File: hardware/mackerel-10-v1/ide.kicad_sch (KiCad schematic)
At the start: 12 parts, among them J14 Screw_Terminal_01x04, J3 Conn_02x20_Odd_Even, U12 74HC245, U13 74HC245

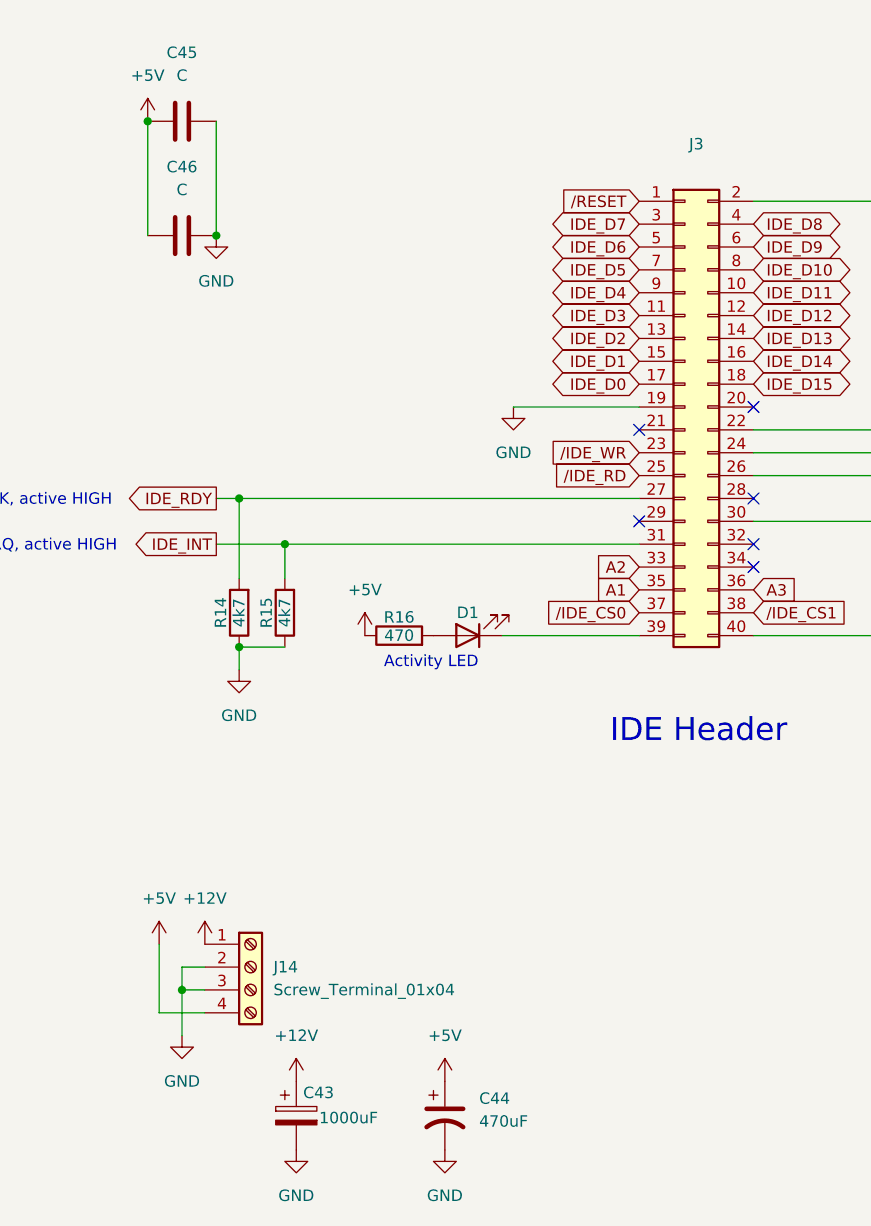
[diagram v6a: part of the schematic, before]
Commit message: Remove BERR from CPLD
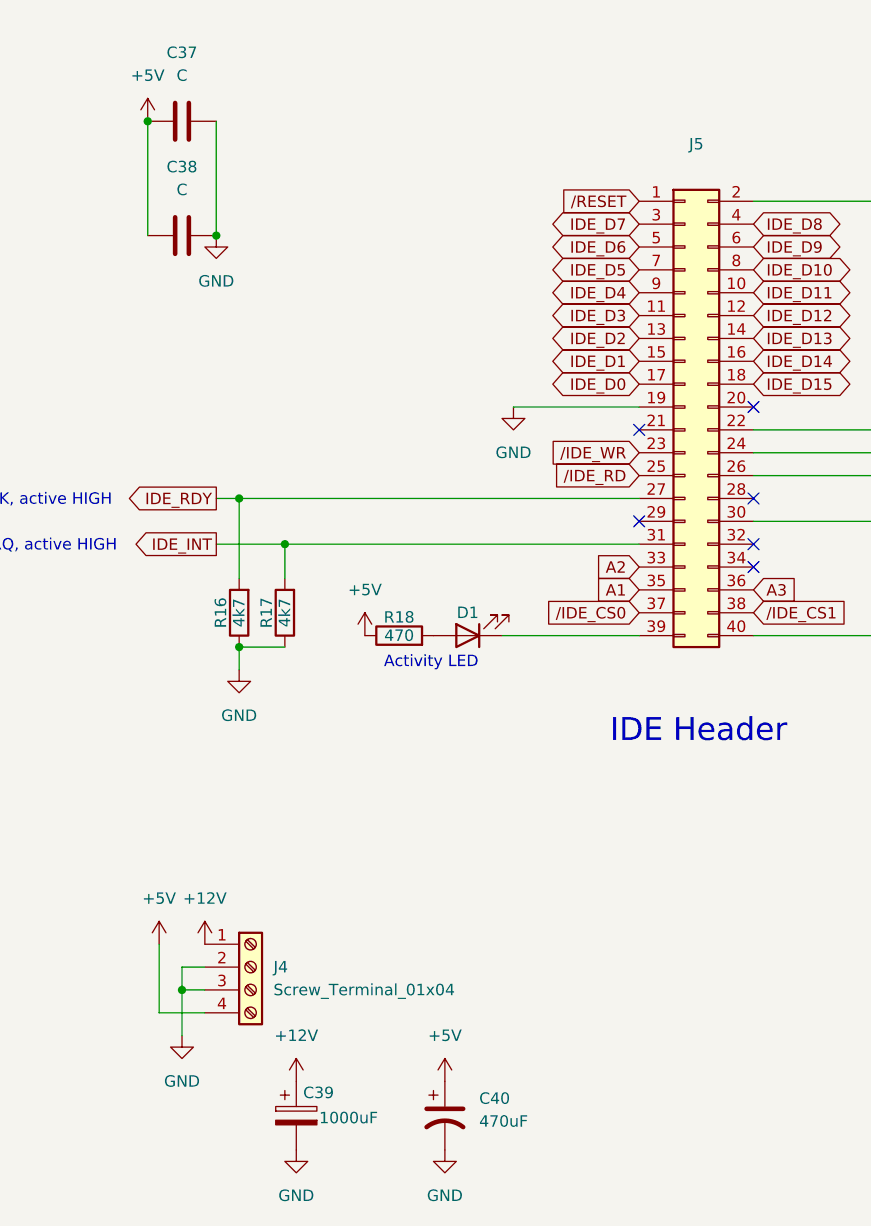
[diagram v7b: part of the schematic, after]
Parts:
- renumbered C45 to C37, C46 to C38, C43 to C39, C44 to C40, J14 to J4, J3 to J5, R14 to R16, R15 to R17, R16 to R18
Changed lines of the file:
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@@
 		(dnp no)
 		(fields_autoplaced yes)
-		(property "Reference" "J3"
+		(property "Reference" "J5"
 			(at 190.5 41.91 0)
 			(effects
@@
 			(project "mackerel-10-v1"
 				(path "/0a8f74be-008b-4256-a2d9-73a458311ea0/159c02d4-7185-497f-a123-96b594aecd43"
-					(reference "J3")
+					(reference "J5")
 					(unit 1)
 				)
@@
 		(dnp no)
 		(fields_autoplaced yes)
-		(property "Reference" "#PWR0102"
+		(property "Reference" "#PWR058"
 			(at 133.35 147.32 0)
 			(effects
@@
 			(project ""
 				(path "/0a8f74be-008b-4256-a2d9-73a458311ea0/159c02d4-7185-497f-a123-96b594aecd43"
-					(reference "#PWR0102")
+					(reference "#PWR058")
 					(unit 1)
 				)
@@
 		(dnp no)
 		(fields_autoplaced yes)
-		(property "Reference" "#PWR044"
+		(property "Reference" "#PWR064"
 			(at 153.67 100.33 0)
 			(effects
@@
 			(project "mackerel-10-v1"
 				(path "/0a8f74be-008b-4256-a2d9-73a458311ea0/159c02d4-7185-497f-a123-96b594aecd43"
-					(reference "#PWR044")
+					(reference "#PWR064")
 					(unit 1)
 				)
@@
 		(dnp no)
 		(fields_autoplaced yes)
-		(property "Reference" "C44"
+		(property "Reference" "C40"
 			(at 166.37 147.9549 0)
 			(effects
@@
 			(project "mackerel-10-v1"
 				(path "/0a8f74be-008b-4256-a2d9-73a458311ea0/159c02d4-7185-497f-a123-96b594aecd43"
-					(reference "C44")
+					(reference "C40")
 					(unit 1)
 				)
@@
 		(dnp no)
 		(fields_autoplaced yes)
-		(property "Reference" "C46"
+		(property "Reference" "C38"
 			(at 133.35 44.45 90)
 			(effects
@@
 			(project "mackerel-10-v1"
 				(path "/0a8f74be-008b-4256-a2d9-73a458311ea0/159c02d4-7185-497f-a123-96b594aecd43"
-					(reference "C46")
+					(reference "C38")
 					(unit 1)
 				)
@@
 		(dnp no)
 		(fields_autoplaced yes)
-		(property "Reference" "#PWR040"
+		(property "Reference" "#PWR053"
 			(at 68.58 81.28 0)
 			(effects
@@
 			(project "mackerel-10-v1"
 				(path "/0a8f74be-008b-4256-a2d9-73a458311ea0/159c02d4-7185-497f-a123-96b594aecd43"
-					(reference "#PWR040")
+					(reference "#PWR053")
 					(unit 1)
 				)
@@
 		(dnp no)
 		(fields_autoplaced yes)
-		(property "Reference" "#PWR096"
+		(property "Reference" "#PWR056"
 			(at 129.54 43.18 0)
 			(effects
@@
 			(project "mackerel-10-v1"
 				(path "/0a8f74be-008b-4256-a2d9-73a458311ea0/159c02d4-7185-497f-a123-96b594aecd43"
-					(reference "#PWR096")
+					(reference "#PWR056")
 					(unit 1)
 				)
@@
 		(on_board yes)
 		(dnp no)
-		(property "Reference" "R15"
+		(property "Reference" "R17"
 			(at 142.748 93.98 90)
 			(effects
@@
 			(project "mackerel-10-v1"
 				(path "/0a8f74be-008b-4256-a2d9-73a458311ea0/159c02d4-7185-497f-a123-96b594aecd43"
-					(reference "R15")
+					(reference "R17")
 					(unit 1)
 				)
@@
 		(dnp no)
 		(fields_autoplaced yes)
-		(property "Reference" "#PWR0100"
+		(property "Reference" "#PWR059"
 			(at 135.89 134.62 0)
 			(effects
@@
 			(project ""
 				(path "/0a8f74be-008b-4256-a2d9-73a458311ea0/159c02d4-7185-497f-a123-96b594aecd43"
-					(reference "#PWR0100")
+					(reference "#PWR059")
 					(unit 1)
 				)
@@
 		(dnp no)
 		(fields_autoplaced yes)
-		(property "Reference" "#PWR071"
+		(property "Reference" "#PWR062"
 			(at 146.05 149.86 0)
 			(effects
@@
 			(project "mackerel-10-v1"
 				(path "/0a8f74be-008b-4256-a2d9-73a458311ea0/159c02d4-7185-497f-a123-96b594aecd43"
-					(reference "#PWR071")
+					(reference "#PWR062")
 					(unit 1)
 				)
@@
 		(dnp no)
 		(fields_autoplaced yes)
-		(property "Reference" "J14"
+		(property "Reference" "J4"
 			(at 143.51 133.3499 0)
 			(effects
@@
 			(project ""
 				(path "/0a8f74be-008b-4256-a2d9-73a458311ea0/159c02d4-7185-497f-a123-96b594aecd43"
-					(reference "J14")
+					(reference "J4")
 					(unit 1)
 				)
@@
 		(on_board yes)
 		(dnp no)
-		(property "Reference" "R14"
+		(property "Reference" "R16"
 			(at 137.668 93.98 90)
 			(effects
@@
 			(project "mackerel-10-v1"
 				(path "/0a8f74be-008b-4256-a2d9-73a458311ea0/159c02d4-7185-497f-a123-96b594aecd43"
-					(reference "R14")
+					(reference "R16")
 					(unit 1)
 				)
@@
 		(dnp no)
 		(fields_autoplaced yes)
-		(property "Reference" "#PWR045"
+		(property "Reference" "#PWR067"
 			(at 170.18 77.47 0)
 			(effects
@@
 			(project "mackerel-10-v1"
 				(path "/0a8f74be-008b-4256-a2d9-73a458311ea0/159c02d4-7185-497f-a123-96b594aecd43"
-					(reference "#PWR045")
+					(reference "#PWR067")
 					(unit 1)
 				)
@@
 		(on_board yes)
 		(dnp no)
-		(property "Reference" "C43"
+		(property "Reference" "C39"
 			(at 146.812 147.32 0)
 			(effects
@@
 			(project "mackerel-10-v1"
 				(path "/0a8f74be-008b-4256-a2d9-73a458311ea0/159c02d4-7185-497f-a123-96b594aecd43"
-					(reference "C43")
+					(reference "C39")
 					(unit 1)
 				)
@@
 		(dnp no)
 		(fields_autoplaced yes)
-		(property "Reference" "#PWR095"
+		(property "Reference" "#PWR066"
 			(at 162.56 160.02 0)
 			(effects
@@
 			(project "mackerel-10-v1"
 				(path "/0a8f74be-008b-4256-a2d9-73a458311ea0/159c02d4-7185-497f-a123-96b594aecd43"
-					(reference "#PWR095")
+					(reference "#PWR066")
 					(unit 1)
 				)
@@
 		(dnp no)
 		(fields_autoplaced yes)
-		(property "Reference" "C45"
+		(property "Reference" "C37"
 			(at 133.35 31.75 90)
 			(effects
@@
 			(project "mackerel-10-v1"
 				(path "/0a8f74be-008b-4256-a2d9-73a458311ea0/159c02d4-7185-497f-a123-96b594aecd43"
-					(reference "C45")
+					(reference "C37")
 					(unit 1)
 				)
@@
 		(dnp no)
 		(fields_autoplaced yes)
-		(property "Reference" "#PWR039"
+		(property "Reference" "#PWR052"
 			(at 68.58 38.1 0)
 			(effects
@@
 			(project "mackerel-10-v1"
 				(path "/0a8f74be-008b-4256-a2d9-73a458311ea0/159c02d4-7185-497f-a123-96b594aecd43"
-					(reference "#PWR039")
+					(reference "#PWR052")
 					(unit 1)
 				)
@@
 		(dnp no)
 		(fields_autoplaced yes)
-		(property "Reference" "#PWR074"
+		(property "Reference" "#PWR063"
 			(at 146.05 160.02 0)
 			(effects
@@
 			(project "mackerel-10-v1"
 				(path "/0a8f74be-008b-4256-a2d9-73a458311ea0/159c02d4-7185-497f-a123-96b594aecd43"
-					(reference "#PWR074")
+					(reference "#PWR063")
 					(unit 1)
 				)
@@
 		(dnp no)
 		(fields_autoplaced yes)
-		(property "Reference" "#PWR046"
+		(property "Reference" "#PWR068"
 			(at 219.71 107.95 0)
 			(effects
@@
 			(project "mackerel-10-v1"
 				(path "/0a8f74be-008b-4256-a2d9-73a458311ea0/159c02d4-7185-497f-a123-96b594aecd43"
-					(reference "#PWR046")
+					(reference "#PWR068")
 					(unit 1)
 				)
@@
 		(dnp no)
 		(fields_autoplaced yes)
-		(property "Reference" "#PWR041"
+		(property "Reference" "#PWR054"
 			(at 68.58 111.76 0)
 			(effects
@@
 			(project "mackerel-10-v1"
 				(path "/0a8f74be-008b-4256-a2d9-73a458311ea0/159c02d4-7185-497f-a123-96b594aecd43"
-					(reference "#PWR041")
+					(reference "#PWR054")
 					(unit 1)
 				)
@@
 		(dnp no)
 		(fields_autoplaced yes)
-		(property "Reference" "#PWR097"
+		(property "Reference" "#PWR060"
 			(at 137.16 58.42 0)
 			(effects
@@
 			(project "mackerel-10-v1"
 				(path "/0a8f74be-008b-4256-a2d9-73a458311ea0/159c02d4-7185-497f-a123-96b594aecd43"
-					(reference "#PWR097")
+					(reference "#PWR060")
 					(unit 1)
 				)
@@
 		(dnp no)
 		(fields_autoplaced yes)
-		(property "Reference" "#PWR083"
+		(property "Reference" "#PWR065"
 			(at 162.56 149.86 0)
 			(effects
@@
 			(project "mackerel-10-v1"
 				(path "/0a8f74be-008b-4256-a2d9-73a458311ea0/159c02d4-7185-497f-a123-96b594aecd43"
-					(reference "#PWR083")
+					(reference "#PWR065")
 					(unit 1)
 				)
@@
 		(dnp no)
 		(fields_autoplaced yes)
-		(property "Reference" "#PWR042"
+		(property "Reference" "#PWR055"
 			(at 68.58 154.94 0)
 			(effects
@@
 			(project "mackerel-10-v1"
 				(path "/0a8f74be-008b-4256-a2d9-73a458311ea0/159c02d4-7185-497f-a123-96b594aecd43"
-					(reference "#PWR042")
+					(reference "#PWR055")
 					(unit 1)
 				)
@@
 		(dnp no)
 		(fields_autoplaced yes)
-		(property "Reference" "#PWR043"
+		(property "Reference" "#PWR061"
 			(at 139.7 106.68 0)
 			(effects
@@
 			(project "mackerel-10-v1"
 				(path "/0a8f74be-008b-4256-a2d9-73a458311ea0/159c02d4-7185-497f-a123-96b594aecd43"
-					(reference "#PWR043")
+					(reference "#PWR061")
 					(unit 1)
 				)
@@
 		(dnp no)
 		(fields_autoplaced yes)
-		(property "Reference" "#PWR0101"
+		(property "Reference" "#PWR057"
 			(at 130.81 134.62 0)
 			(effects
@@
 			(project ""
 				(path "/0a8f74be-008b-4256-a2d9-73a458311ea0/159c02d4-7185-497f-a123-96b594aecd43"
-					(reference "#PWR0101")
+					(reference "#PWR057")
 					(unit 1)
 				)
@@
 		(on_board yes)
 		(dnp no)
-		(property "Reference" "R16"
+		(property "Reference" "R18"
 			(at 157.48 94.488 90)
 			(effects
@@
 			(project "mackerel-10-v1"
 				(path "/0a8f74be-008b-4256-a2d9-73a458311ea0/159c02d4-7185-497f-a123-96b594aecd43"
-					(reference "R16")
-					(unit 1)
-				)
+					(reference "R18")
+					(unit 1)
+				)

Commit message: Mackerel-10 v1.1 release PCB
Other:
- title: Mackerel-10 SBC v1 -> Mackerel-10 SBC v1.1
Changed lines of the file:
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@@
 	(paper "A")
 	(title_block
-		(title "Mackerel-10 SBC v1")
-		(date "2024-09-23")
-		(rev "1.0a")
+		(title "Mackerel-10 SBC v1.1")
+		(date "2024-10-27")
+		(rev "1.1a")
 		(company "Colin Maykish")
 	)
